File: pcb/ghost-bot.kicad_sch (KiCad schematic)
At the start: 33 parts, among them J1 Conn_01x03_Pin, J2 Conn_01x03_Pin, J3 Conn_01x04_Pin, J4 Conn_01x02_Pin, SW1 SW_Push, SW2 SW_Push, SW3 SW_SPDT

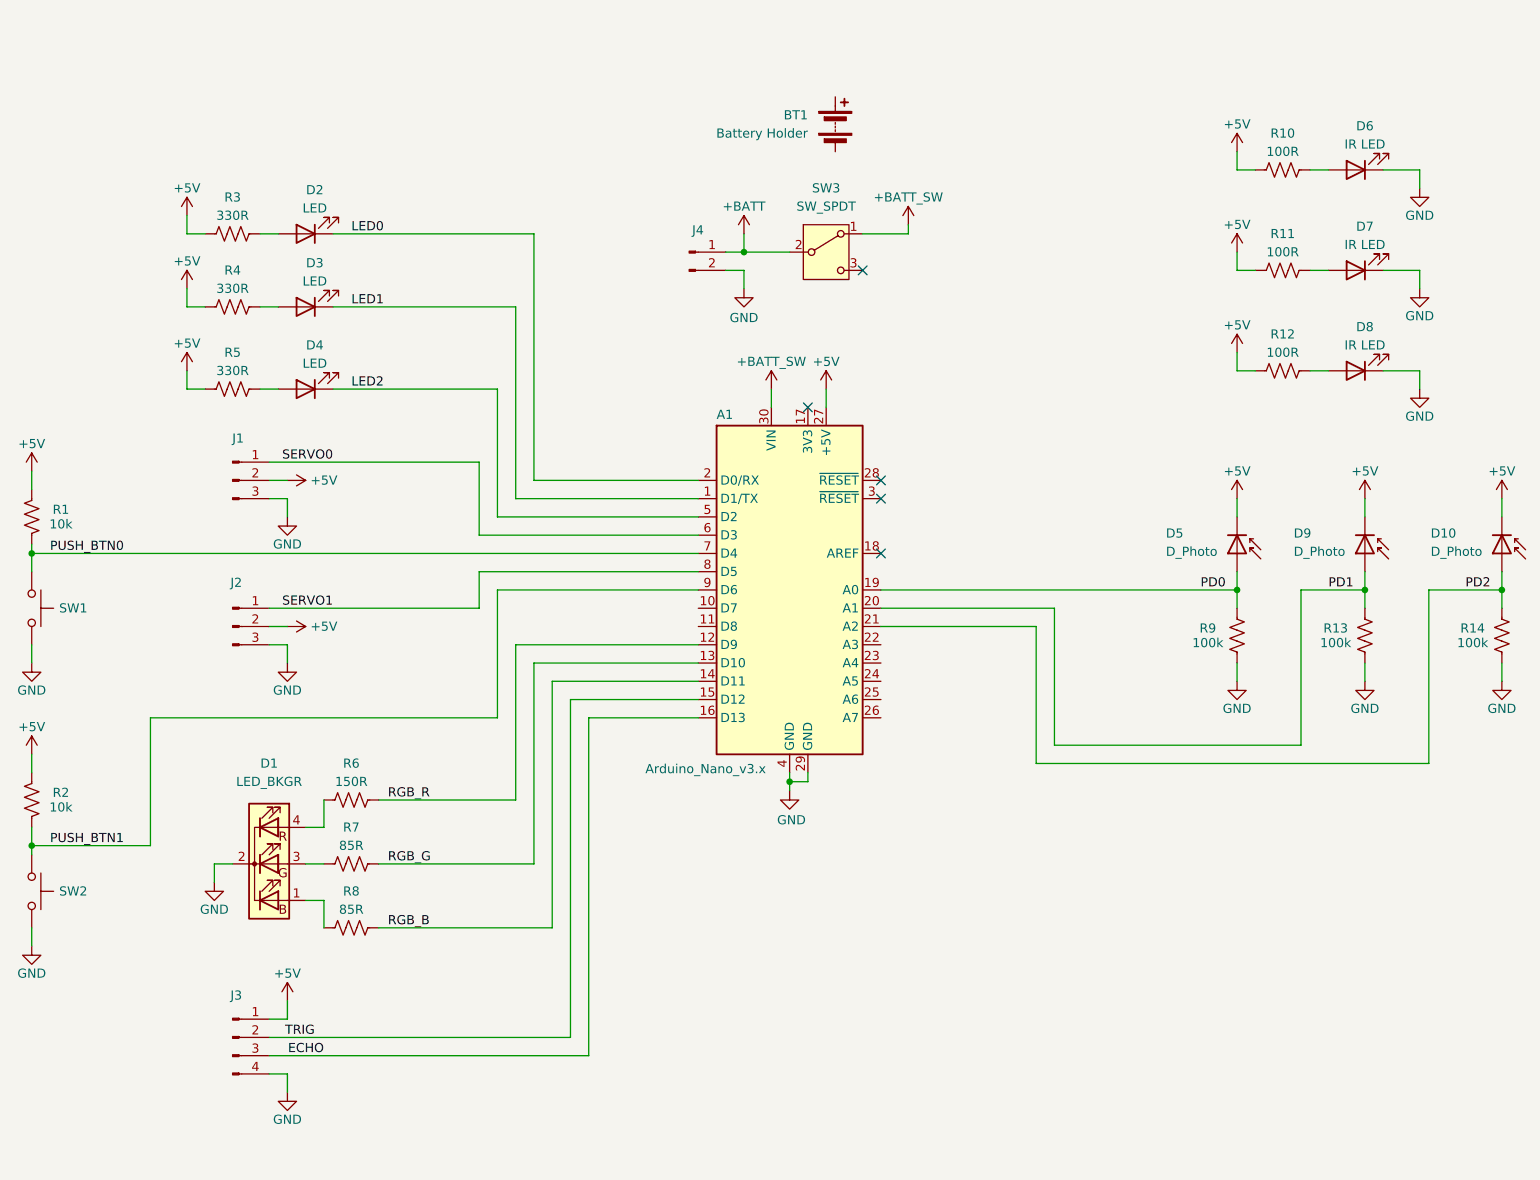
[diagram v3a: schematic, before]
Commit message: Add footprints for servos
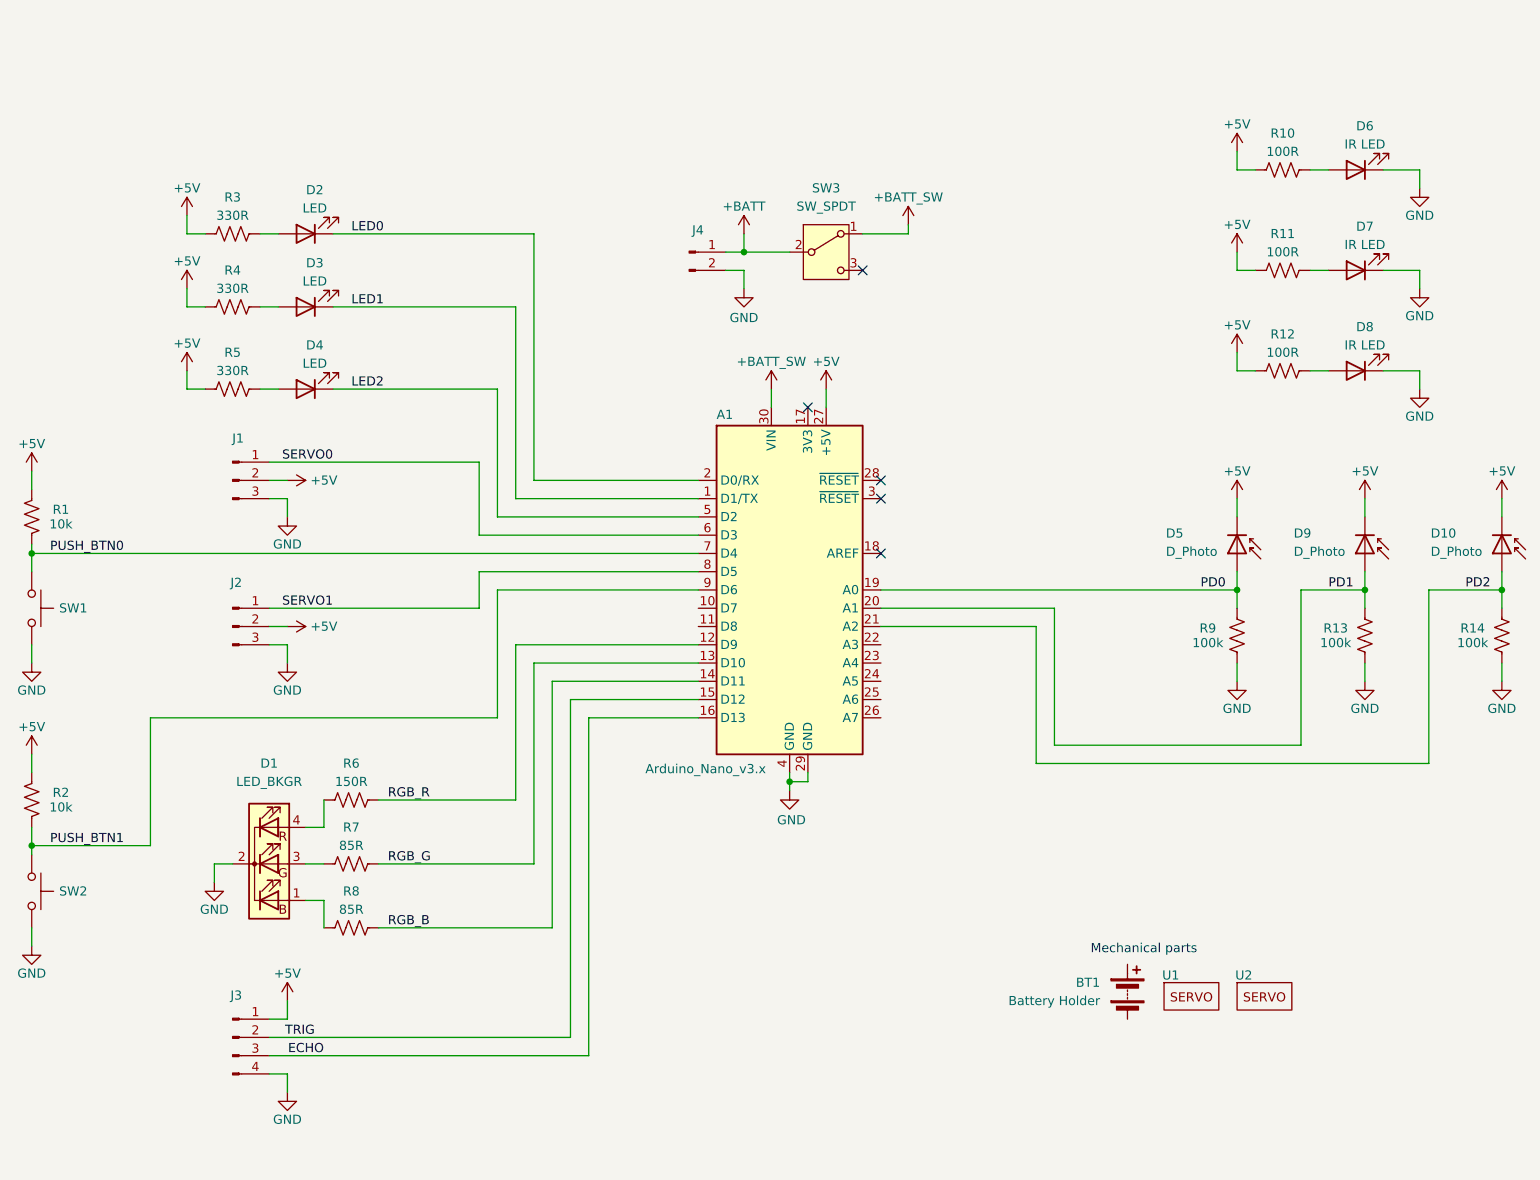
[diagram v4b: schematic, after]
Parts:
- added U1, U2: ~, ghost-bot-footprints:SG90 Mount, symbol ghost-bot-symbols:Servo Mechanical
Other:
- note added: "Mechanical parts"
- moved on the sheet: BT1
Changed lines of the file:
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@@
+		)
+	)
+	(text "Mechanical parts"
+		(exclude_from_sim no)
+		(at 197.866 146.558 0)
+		(effects
+			(font
+				(size 1.27 1.27)
+			)
 		)
 	)
@@
 	(symbol
 		(lib_id "ghost-bot-symbols:Battery Holder")
-		(at 154.94 31.75 0)
+		(at 195.58 152.4 0)
 		(unit 1)
 		(exclude_from_sim no)
@@
 		(dnp no)
 		(property "Reference" "BT1"
-			(at 151.13 30.4799 0)
+			(at 191.77 151.1299 0)
 			(effects
 				(font
@@
 		)
 		(property "Value" "Battery Holder"
-			(at 151.13 33.0199 0)
+			(at 191.77 153.6699 0)
 			(effects
 				(font
@@
 		)
 		(property "Footprint" "ghost-bot-footprints:Keystone 2478 Battery Holder"
-			(at 154.94 30.226 90)
+			(at 195.58 150.876 90)
 			(effects
 				(font
@@
 		)
 		(property "Datasheet" "~"
-			(at 154.94 30.226 90)
+			(at 195.58 150.876 90)
 			(effects
 				(font
@@
 		)
 		(property "Description" "Multiple-cell battery"
-			(at 154.94 31.75 0)
+			(at 195.58 152.4 0)
 			(effects
 				(font
@@
 	)
 	(symbol
+		(lib_id "ghost-bot-symbols:Servo Mechanical")
+		(at 210.82 151.13 0)
+		(unit 1)
+		(exclude_from_sim no)
+		(in_bom yes)
+		(on_board yes)
+		(dnp no)
+		(property "Reference" "U2"
+			(at 210.566 150.114 0)
+			(effects
+				(font
+					(size 1.27 1.27)
+				)
+				(justify left)
+			)
+		)
+		(property "Value" "~"
+			(at 219.71 154.305 0)
+			(effects
+				(font
+					(size 1.27 1.27)
+				)
+				(justify left)
+			)
+		)
+		(property "Footprint" "ghost-bot-footprints:SG90 Mount"
+			(at 210.82 151.13 0)
+			(effects
+				(font
+					(size 1.27 1.27)
+				)
+				(hide yes)
+			)
+		)
+		(property "Datasheet" ""
+			(at 210.82 151.13 0)
+			(effects
+				(font
+					(size 1.27 1.27)
+				)
+				(hide yes)
+			)
+		)
+		(property "Description" ""
+			(at 210.82 151.13 0)
+			(effects
+				(font
+					(size 1.27 1.27)
+				)
+				(hide yes)
+			)
+		)
+		(instances
+			(project "ghost-bot"
+				(path "/9de140fd-a546-4656-a97e-49be7c9777a1"
+					(reference "U2")
+					(unit 1)
+				)
+			)
+		)
+	)
+	(symbol
 		(lib_id "Device:R_US")
 		(at 71.12 46.99 90)
@@
 					(unit 1)
 				)
+			)
+		)
+	)
+	(symbol
+		(lib_id "ghost-bot-symbols:Servo Mechanical")
+		(at 200.66 151.13 0)
+		(unit 1)
+		(exclude_from_sim no)
+		(in_bom yes)
+		(on_board yes)
+		(dnp no)
+		(property "Reference" "U1"
+			(at 200.406 150.114 0)
+			(effects
+				(font
+					(size 1.27 1.27)
+				)
+				(justify left)
+			)
+		)
+		(property "Value" "~"
+			(at 209.55 154.305 0)
+			(effects
+				(font
+					(size 1.27 1.27)
+				)
+				(justify left)
+			)
+		)
+		(property "Footprint" "ghost-bot-footprints:SG90 Mount"
+			(at 200.66 151.13 0)
+			(effects
+				(font
+					(size 1.27 1.27)
+				)
+				(hide yes)
+			)
+		)
+		(property "Datasheet" ""
+			(at 200.66 151.13 0)
+			(effects
+				(font
+					(size 1.27 1.27)
+				)
+				(hide yes)
+			)
+		)
+		(property "Description" ""
+			(at 200.66 151.13 0)
+			(effects
+				(font
+					(size 1.27 1.27)
+				)
+				(hide yes)
+			)
+		)
+		(instances
+			(project "ghost-bot"
+				(path "/9de140fd-a546-4656-a97e-49be7c9777a1"
+					(reference "U1")
+					(unit 1)
+				)

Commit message: WIP commit before changing layout
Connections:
- net PD2: now also A1.26 (A7); no longer A1.21 (A2)
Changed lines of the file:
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@@
+	(wire
+		(pts
+			(xy 161.29 114.3) (xy 182.88 114.3)
+		)
+		(stroke
+			(width 0)
+			(type default)
+		)
+	)
 	(wire
 		(pts
@@
 	(wire
 		(pts
-			(xy 182.88 101.6) (xy 182.88 120.65)
-		)
-		(stroke
-			(width 0)
-			(type default)
-		)
-	)
-	(wire
-		(pts
 			(xy 135.89 81.28) (xy 113.03 81.28)
 		)
@@
 	(wire
 		(pts
+			(xy 182.88 114.3) (xy 182.88 120.65)
+		)
+		(stroke
+			(width 0)
+			(type default)
+		)
+	)
+	(wire
+		(pts
 			(xy 231.14 52.07) (xy 236.22 52.07)
 		)
 		(stroke
-			(width 0)
-			(type default)
-		)
-	)
-	(wire
-		(pts
-			(xy 161.29 101.6) (xy 182.88 101.6)
-		)
-		(stroke

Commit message: Add initial routing
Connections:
- net PD1: now also A1.25 (A6); no longer A1.20 (A1)
- net RGB_B: now also A1.12 (D9); no longer A1.14 (D11)
- net RGB_R: now also A1.14 (D11); no longer A1.12 (D9)

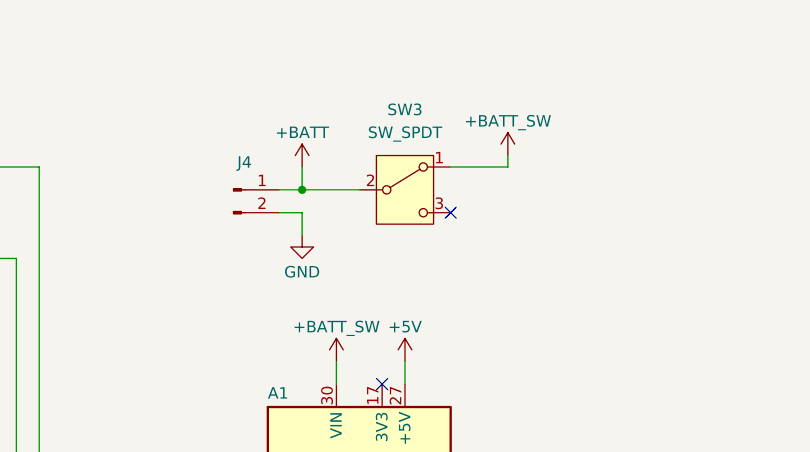
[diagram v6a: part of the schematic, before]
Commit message: Update power switch
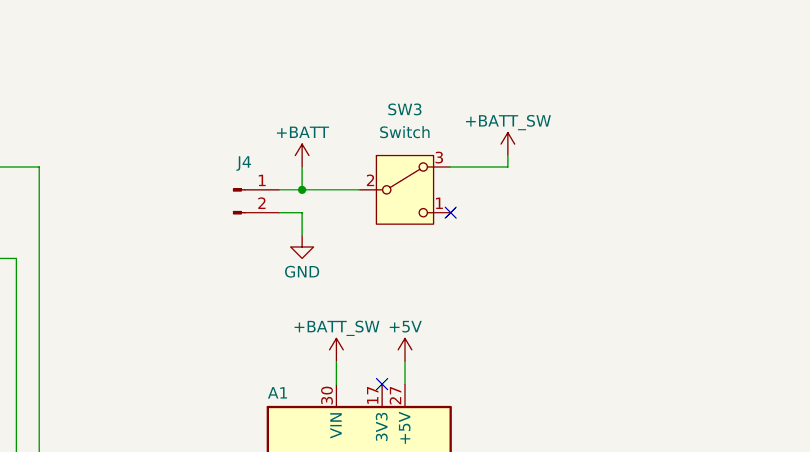
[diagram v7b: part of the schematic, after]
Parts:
- removed SW3: SW_SPDT, Button_Switch_THT:SW_Slide_SPDT_Straight_CK_OS102011MS2Q, symbol Switch:SW_SPDT
- added SW3: Switch, Button_Switch_THT:SW_E-Switch_EG1271_SPDT, symbol ghost-bot-symbols:Switch
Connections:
- net +BATT: now also SW3.2 (B)
- net +BATT_SW: now also SW3.3 (A)
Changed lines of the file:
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@@
+	)
+	(symbol
+		(lib_id "ghost-bot-symbols:Switch")
+		(at 153.67 49.53 0)
+		(unit 1)
+		(exclude_from_sim no)
+		(in_bom yes)
+		(on_board yes)
+		(dnp no)
+		(fields_autoplaced yes)
+		(property "Reference" "SW3"
+			(at 153.67 40.64 0)
+			(effects
+				(font
+					(size 1.27 1.27)
+				)
+			)
+		)
+		(property "Value" "Switch"
+			(at 153.67 43.18 0)
+			(effects
+				(font
+					(size 1.27 1.27)
+				)
+			)
+		)
+		(property "Footprint" "Button_Switch_THT:SW_E-Switch_EG1271_SPDT"
+			(at 153.67 59.69 0)
+			(effects
+				(font
+					(size 1.27 1.27)
+				)
+				(hide yes)
+			)
+		)
+		(property "Datasheet" "~"
+			(at 153.67 57.15 0)
+			(effects
+				(font
+					(size 1.27 1.27)
+				)
+				(hide yes)
+			)
+		)
+		(property "Description" "Switch, single pole double throw"
+			(at 153.67 49.53 0)
+			(effects
+				(font
+					(size 1.27 1.27)
+				)
+				(hide yes)
+			)
+		)
+		(pin "3"
+		)
+		(pin "1"
+		)
+		(pin "5"
+		)
+		(pin "4"
+		)
+		(pin "2"
+		)
+		(pin "6"
+		)
+		(instances
+			(project "ghost-bot"
+				(path "/9de140fd-a546-4656-a97e-49be7c9777a1"
+					(reference "SW3")
+					(unit 1)
+				)
+			)
+		)
 	)
 	(symbol
@@
 					(unit 1)
 				)
-			)
-		)
-	)
-	(symbol
-		(lib_id "Switch:SW_SPDT")
-		(at 153.67 49.53 0)
-		(unit 1)
-		(exclude_from_sim no)
-		(in_bom yes)
-		(on_board yes)
-		(dnp no)
-		(fields_autoplaced yes)
-		(property "Reference" "SW3"
-			(at 153.67 40.64 0)
-			(effects
-				(font
-					(size 1.27 1.27)
-				)
-			)
-		)
-		(property "Value" "SW_SPDT"
-			(at 153.67 43.18 0)
-			(effects
-				(font
-					(size 1.27 1.27)
-				)
-			)
-		)
-		(property "Footprint" "Button_Switch_THT:SW_Slide_SPDT_Straight_CK_OS102011MS2Q"
-			(at 153.67 49.53 0)
-			(effects
-				(font
-					(size 1.27 1.27)
-				)
-				(hide yes)
-			)
-		)
-		(property "Datasheet" "~"
-			(at 153.67 57.15 0)
-			(effects
-				(font
-					(size 1.27 1.27)
-				)
-				(hide yes)
-			)
-		)
-		(property "Description" "Switch, single pole double throw"
-			(at 153.67 49.53 0)
-			(effects
-				(font
-					(size 1.27 1.27)
-				)
-				(hide yes)
-			)
-		)
-		(pin "3"
-		)
-		(pin "1"
-		)
-		(pin "2"
-		)
-		(instances
-			(project "ghost-bot"
-				(path "/9de140fd-a546-4656-a97e-49be7c9777a1"
-					(reference "SW3")
-					(unit 1)
-				)

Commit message: Fix servo 3d model, add battery holder 3d model
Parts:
- U1: footprint ghost-bot-footprints:SG90 Mount -> ghost-bot-footprints:SG90 Mount Left
- U2: footprint ghost-bot-footprints:SG90 Mount -> ghost-bot-footprints:SG90 Mount Right
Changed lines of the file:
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@@
 			)
 		)
-		(property "Footprint" "ghost-bot-footprints:SG90 Mount"
+		(property "Footprint" "ghost-bot-footprints:SG90 Mount Right"
 			(at 210.82 151.13 0)
 			(effects
@@
 			)
 		)
-		(property "Footprint" "ghost-bot-footprints:SG90 Mount"
+		(property "Footprint" "ghost-bot-footprints:SG90 Mount Left"
 			(at 200.66 151.13 0)
 			(effects
